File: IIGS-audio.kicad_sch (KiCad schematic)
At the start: 41 parts, among them J1 Conn_01x07, J2 SJ1-3515N, J4 Conn_01x02_Male, U1 MC14052BDR2G, U2 TL084

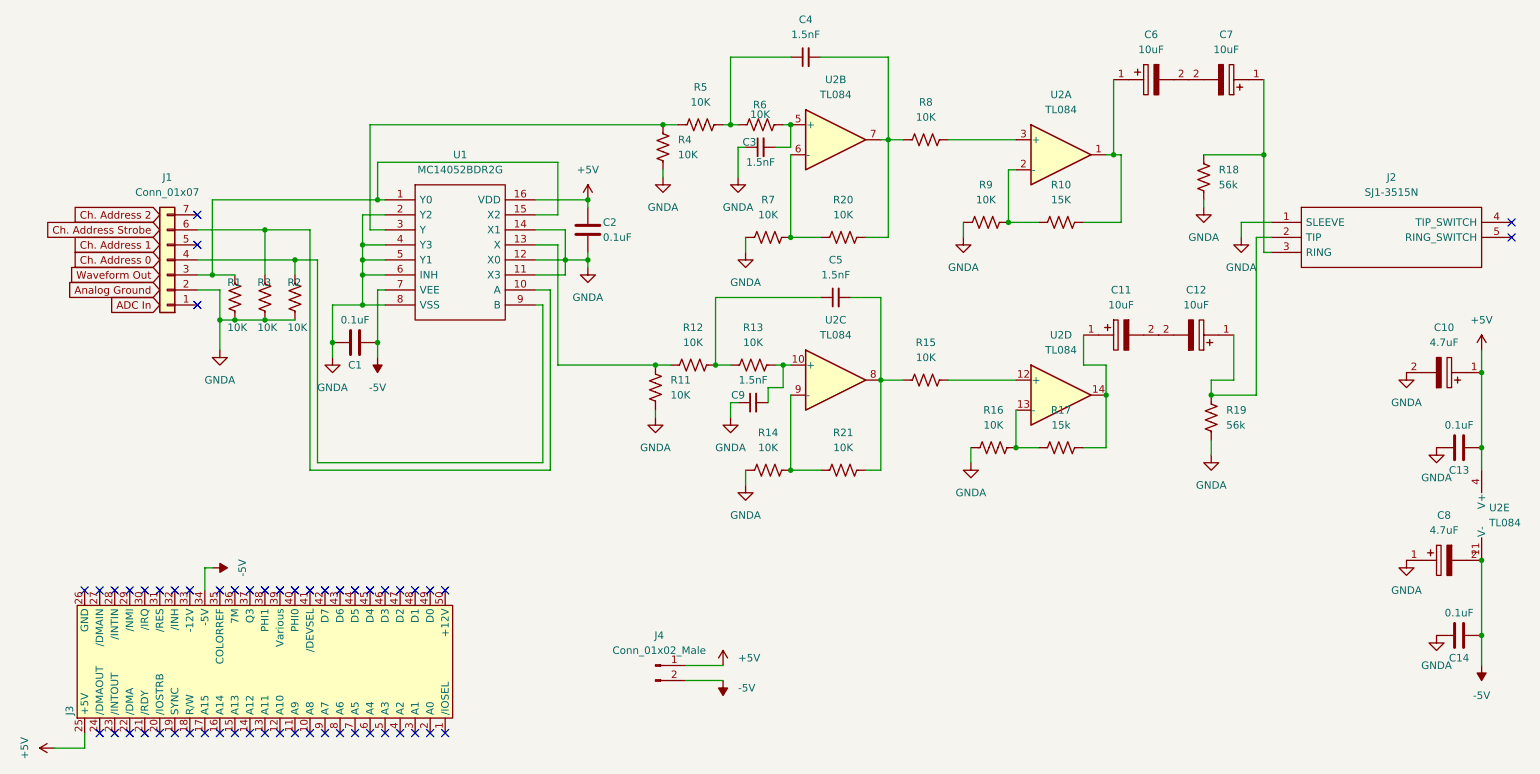
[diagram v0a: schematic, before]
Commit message: minor tweaks, got rid of PSU rail caps because they contributed to noise
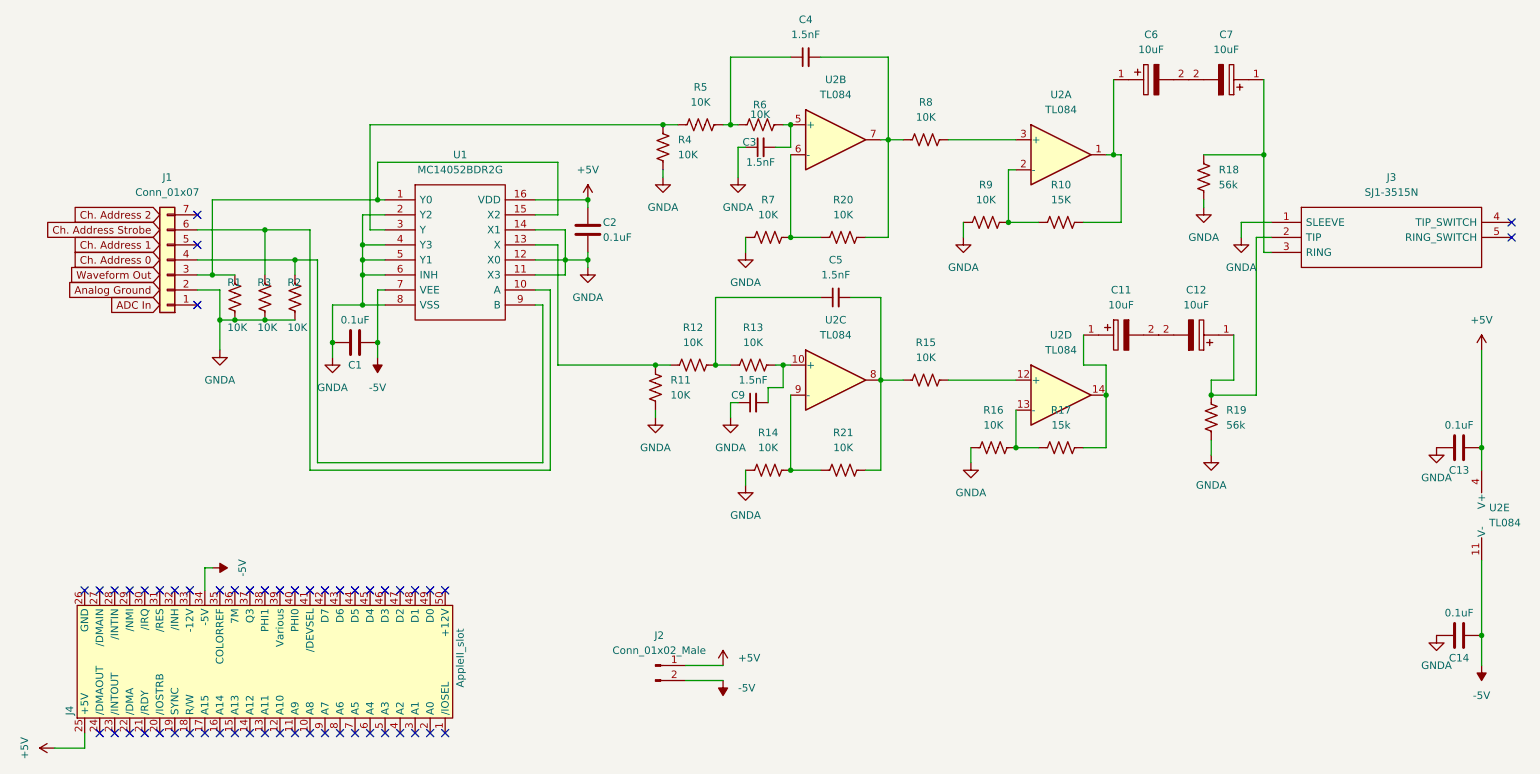
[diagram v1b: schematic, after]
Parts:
- removed C10, C8: 4.7uF, CAPAE430X610N, symbol SamacSys_Parts:VZT100M1HTR-0406
- J4: renamed from J3; value (none) -> AppleII_slot; footprint (none) -> Apple2:Apple2_card_slot
- renumbered J4 to J2, J2 to J3
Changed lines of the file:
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@@
   (junction (at 149.86 121.92) (diameter 0) (color 0 0 0 0)
   )
-  (junction (at 266.7 105.41) (diameter 0) (color 0 0 0 0)
-  )
   (junction (at 137.16 104.14) (diameter 0) (color 0 0 0 0)
   )
@@
   )
   (junction (at 220.98 109.22) (diameter 0) (color 0 0 0 0)
-  )
-  (junction (at 266.7 137.16) (diameter 0) (color 0 0 0 0)
   )
   (junction (at 60.96 96.52) (diameter 0) (color 0 0 0 0)
@@
     (stroke (width 0) (type default) (color 0 0 0 0))
   )
-  (wire (pts (xy 266.7 101.6) (xy 266.7 105.41))
-    (stroke (width 0) (type default) (color 0 0 0 0))
-  )
   (wire (pts (xy 266.7 137.16) (xy 266.7 149.86))
     (stroke (width 0) (type default) (color 0 0 0 0))
@@
     (stroke (width 0) (type default) (color 0 0 0 0))
   )
-  (wire (pts (xy 266.7 105.41) (xy 266.7 118.11))
+  (wire (pts (xy 266.7 101.6) (xy 266.7 118.11))
     (stroke (width 0) (type default) (color 0 0 0 0))
   )
@@
     (pin "2")
   )
-  (symbol (lib_id "power:GNDA") (at 254 105.41 0) (unit 1)
-    (in_bom yes) (on_board yes) (fields_autoplaced)
-    (property "Reference" "#PWR01" (id 0) (at 254 111.76 0)
-      (effects (font (size 1.27 1.27)) hide)
-    )
-    (property "Value" "GNDA" (id 1) (at 254 110.49 0))
-    (property "Footprint" "" (id 2) (at 254 105.41 0)
-      (effects (font (size 1.27 1.27)) hide)
-    )
-    (property "Datasheet" "" (id 3) (at 254 105.41 0)
-      (effects (font (size 1.27 1.27)) hide)
-    )
-    (pin "1")
-  )
   (symbol (lib_id "Device:C") (at 115.57 81.28 0) (unit 1)
     (in_bom yes) (on_board yes)
@@
   (symbol (lib_id "Connector:Conn_01x02_Male") (at 127 154.94 0) (unit 1)
     (in_bom yes) (on_board yes) (fields_autoplaced)
-    (property "Reference" "J4" (id 0) (at 127.635 149.86 0))
+    (property "Reference" "J2" (id 0) (at 127.635 149.86 0))
     (property "Value" "Conn_01x02_Male" (id 1) (at 127.635 152.4 0))
     (property "Footprint" "Connector_PinHeader_2.54mm:PinHeader_1x02_P2.54mm_Vertical" (id 2) (at 127 154.94 0)
@@
     (pin "2")
   )
-  (symbol (lib_id "power:GNDA") (at 254 137.16 0) (unit 1)
-    (in_bom yes) (on_board yes) (fields_autoplaced)
-    (property "Reference" "#PWR02" (id 0) (at 254 143.51 0)
-      (effects (font (size 1.27 1.27)) hide)
-    )
-    (property "Value" "GNDA" (id 1) (at 254 142.24 0))
-    (property "Footprint" "" (id 2) (at 254 137.16 0)
-      (effects (font (size 1.27 1.27)) hide)
-    )
-    (property "Datasheet" "" (id 3) (at 254 137.16 0)
-      (effects (font (size 1.27 1.27)) hide)
-    )
-    (pin "1")
-  )
-  (symbol (lib_id "SamacSys_Parts:VZT100M1HTR-0406") (at 254 137.16 0) (unit 1)
-    (in_bom yes) (on_board yes) (fields_autoplaced)
-    (property "Reference" "C8" (id 0) (at 260.35 129.54 0))
-    (property "Value" "4.7uF" (id 1) (at 260.35 132.08 0))
-    (property "Footprint" "CAPAE430X610N" (id 2) (at 262.89 135.89 0)
-      (effects (font (size 1.27 1.27)) (justify left) hide)
-    )
-    (property "Datasheet" "https://www.mouser.co.uk/datasheet/2/231/156315576075-1624351.pdf" (id 3) (at 262.89 138.43 0)
-      (effects (font (size 1.27 1.27)) (justify left) hide)
-    )
-    (property "Description" "Aluminum Electrolytic Capacitors - SMD 10uF 20% 50V Ultra Low ESR" (id 4) (at 262.89 140.97 0)
-      (effects (font (size 1.27 1.27)) (justify left) hide)
-    )
-    (property "Height" "6.1" (id 5) (at 262.89 143.51 0)
-      (effects (font (size 1.27 1.27)) (justify left) hide)
-    )
-    (property "Mouser Part Number" "140-VZT100M1HTR-0406" (id 6) (at 262.89 146.05 0)
-      (effects (font (size 1.27 1.27)) (justify left) hide)
-    )
-    (property "Mouser Price/Stock" "https://www.mouser.co.uk/ProductDetail/Lelon/VZT100M1HTR-0406/?qs=mQP6vorrPAcP1%252BjIAgEecA%3D%3D" (id 7) (at 262.89 148.59 0)
-      (effects (font (size 1.27 1.27)) (justify left) hide)
-    )
-    (property "Manufacturer_Name" "Lelon" (id 8) (at 262.89 151.13 0)
-      (effects (font (size 1.27 1.27)) (justify left) hide)
-    )
-    (property "Manufacturer_Part_Number" "VZT100M1HTR-0406" (id 9) (at 262.89 153.67 0)
-      (effects (font (size 1.27 1.27)) (justify left) hide)
-    )
-    (pin "1")
-    (pin "2")
-  )
   (symbol (lib_id "Device:R_US") (at 66.04 92.71 180) (unit 1)
     (in_bom yes) (on_board yes)
@@
   (symbol (lib_id "appleii_slot:AppleII_slot") (at 92.71 163.83 90) (unit 1)
     (in_bom yes) (on_board yes)
-    (property "Reference" "J3" (id 0) (at 27.94 162.56 0))
-    (property "Value" "" (id 1) (at 93.98 153.67 0))
-    (property "Footprint" "" (id 2) (at 92.71 163.83 0)
+    (property "Reference" "J4" (id 0) (at 27.94 162.56 0))
+    (property "Value" "AppleII_slot" (id 1) (at 93.98 153.67 0))
+    (property "Footprint" "Apple2:Apple2_card_slot" (id 2) (at 92.71 163.83 0)
       (effects (font (size 1.27 1.27)) hide)
     )
@@
     (pin "1")
   )
-  (symbol (lib_id "SamacSys_Parts:VZT100M1HTR-0406") (at 266.7 105.41 180) (unit 1)
-    (in_bom yes) (on_board yes) (fields_autoplaced)
-    (property "Reference" "C10" (id 0) (at 260.35 97.79 0))
-    (property "Value" "4.7uF" (id 1) (at 260.35 100.33 0))
-    (property "Footprint" "CAPAE430X610N" (id 2) (at 257.81 106.68 0)
-      (effects (font (size 1.27 1.27)) (justify left) hide)
-    )
-    (property "Datasheet" "https://www.mouser.co.uk/datasheet/2/231/156315576075-1624351.pdf" (id 3) (at 257.81 104.14 0)
-      (effects (font (size 1.27 1.27)) (justify left) hide)
-    )
-    (property "Description" "Aluminum Electrolytic Capacitors - SMD 10uF 20% 50V Ultra Low ESR" (id 4) (at 257.81 101.6 0)
-      (effects (font (size 1.27 1.27)) (justify left) hide)
-    )
-    (property "Height" "6.1" (id 5) (at 257.81 99.06 0)
-      (effects (font (size 1.27 1.27)) (justify left) hide)
-    )
-    (property "Mouser Part Number" "140-VZT100M1HTR-0406" (id 6) (at 257.81 96.52 0)
-      (effects (font (size 1.27 1.27)) (justify left) hide)
-    )
-    (property "Mouser Price/Stock" "https://www.mouser.co.uk/ProductDetail/Lelon/VZT100M1HTR-0406/?qs=mQP6vorrPAcP1%252BjIAgEecA%3D%3D" (id 7) (at 257.81 93.98 0)
-      (effects (font (size 1.27 1.27)) (justify left) hide)
-    )
-    (property "Manufacturer_Name" "Lelon" (id 8) (at 257.81 91.44 0)
-      (effects (font (size 1.27 1.27)) (justify left) hide)
-    )
-    (property "Manufacturer_Part_Number" "VZT100M1HTR-0406" (id 9) (at 257.81 88.9 0)
-      (effects (font (size 1.27 1.27)) (justify left) hide)
-    )
-    (pin "1")
-    (pin "2")
-  )
   (symbol (lib_id "Device:C") (at 262.89 118.11 90) (unit 1)
     (in_bom yes) (on_board yes)
@@
   (symbol (lib_id "SamacSys_Parts:SJ1-3515N") (at 231.14 80.01 0) (unit 1)
     (in_bom yes) (on_board yes) (fields_autoplaced)
-    (property "Reference" "J2" (id 0) (at 251.46 72.39 0))
+    (property "Reference" "J3" (id 0) (at 251.46 72.39 0))
     (property "Value" "SJ1-3515N" (id 1) (at 251.46 74.93 0))
     (property "Footprint" "SJ13515N" (id 2) (at 267.97 77.47 0)
@@
   )
   (symbol_instances
-    (path "/0e3424c6-01ab-4399-928e-5c701c464000"
-      (reference "#PWR01") (unit 1) (value "GNDA") (footprint "")
-    )
-    (path "/3ebbf65f-f9b7-413b-a86c-4396bf26312a"
-      (reference "#PWR02") (unit 1) (value "GNDA") (footprint "")
-    )
     (path "/77fd3673-00f2-4d58-8bd1-ed055ed8391a"
       (reference "#PWR03") (unit 1) (value "GNDA") (footprint "")
@@
       (reference "C7") (unit 1) (value "10uF") (footprint "CAPAE430X610N")
     )
-    (path "/4075e761-f300-4c80-978c-b9ada572446e"
-      (reference "C8") (unit 1) (value "4.7uF") (footprint "CAPAE430X610N")
-    )
     (path "/23a4c97c-3f20-4dd7-9098-c93ee6d78d1b"
       (reference "C9") (unit 1) (value "1.5nF") (footprint "Capacitor_SMD:C_0603_1608Metric")
     )
-    (path "/7cffe4c2-f26d-4fcb-b1af-4916ea13e751"
-      (reference "C10") (unit 1) (value "4.7uF") (footprint "CAPAE430X610N")
-    )
     (path "/68128f33-bfbc-4f87-9556-7d6316f4edba"
       (reference "C11") (unit 1) (value "10uF") (footprint "CAPAE430X610N")
@@
       (reference "J1") (unit 1) (value "Conn_01x07") (footprint "Connector_PinHeader_2.54mm:PinHeader_1x07_P2.54mm_Horizontal")
     )
+    (path "/17108590-0e42-43c2-ab9e-625e7b4f94b1"
+      (reference "J2") (unit 1) (value "Conn_01x02_Male") (footprint "Connector_PinHeader_2.54mm:PinHeader_1x02_P2.54mm_Vertical")
+    )
     (path "/ff7bfb3a-4870-454e-865a-25334c86ba76"
-      (reference "J2") (unit 1) (value "SJ1-3515N") (footprint "SJ13515N")
+      (reference "J3") (unit 1) (value "SJ1-3515N") (footprint "SJ13515N")
     )
     (path "/66a15523-fdda-4e02-9450-fa8233e5ab05"
-      (reference "J3") (unit 1) (value "AppleII_slot") (footprint "Apple2:Apple2_card_slot")
-    )
-    (path "/17108590-0e42-43c2-ab9e-625e7b4f94b1"
-      (reference "J4") (unit 1) (value "Conn_01x02_Male") (footprint "Connector_PinHeader_2.54mm:PinHeader_1x02_P2.54mm_Vertical")
+      (reference "J4") (unit 1) (value "AppleII_slot") (footprint "Apple2:Apple2_card_slot")
     )
     (path "/2c660256-1140-4d3c-8e60-783fc8e2bf57"
